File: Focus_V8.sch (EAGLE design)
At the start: 103 parts, among them X1 USB+SHIELD

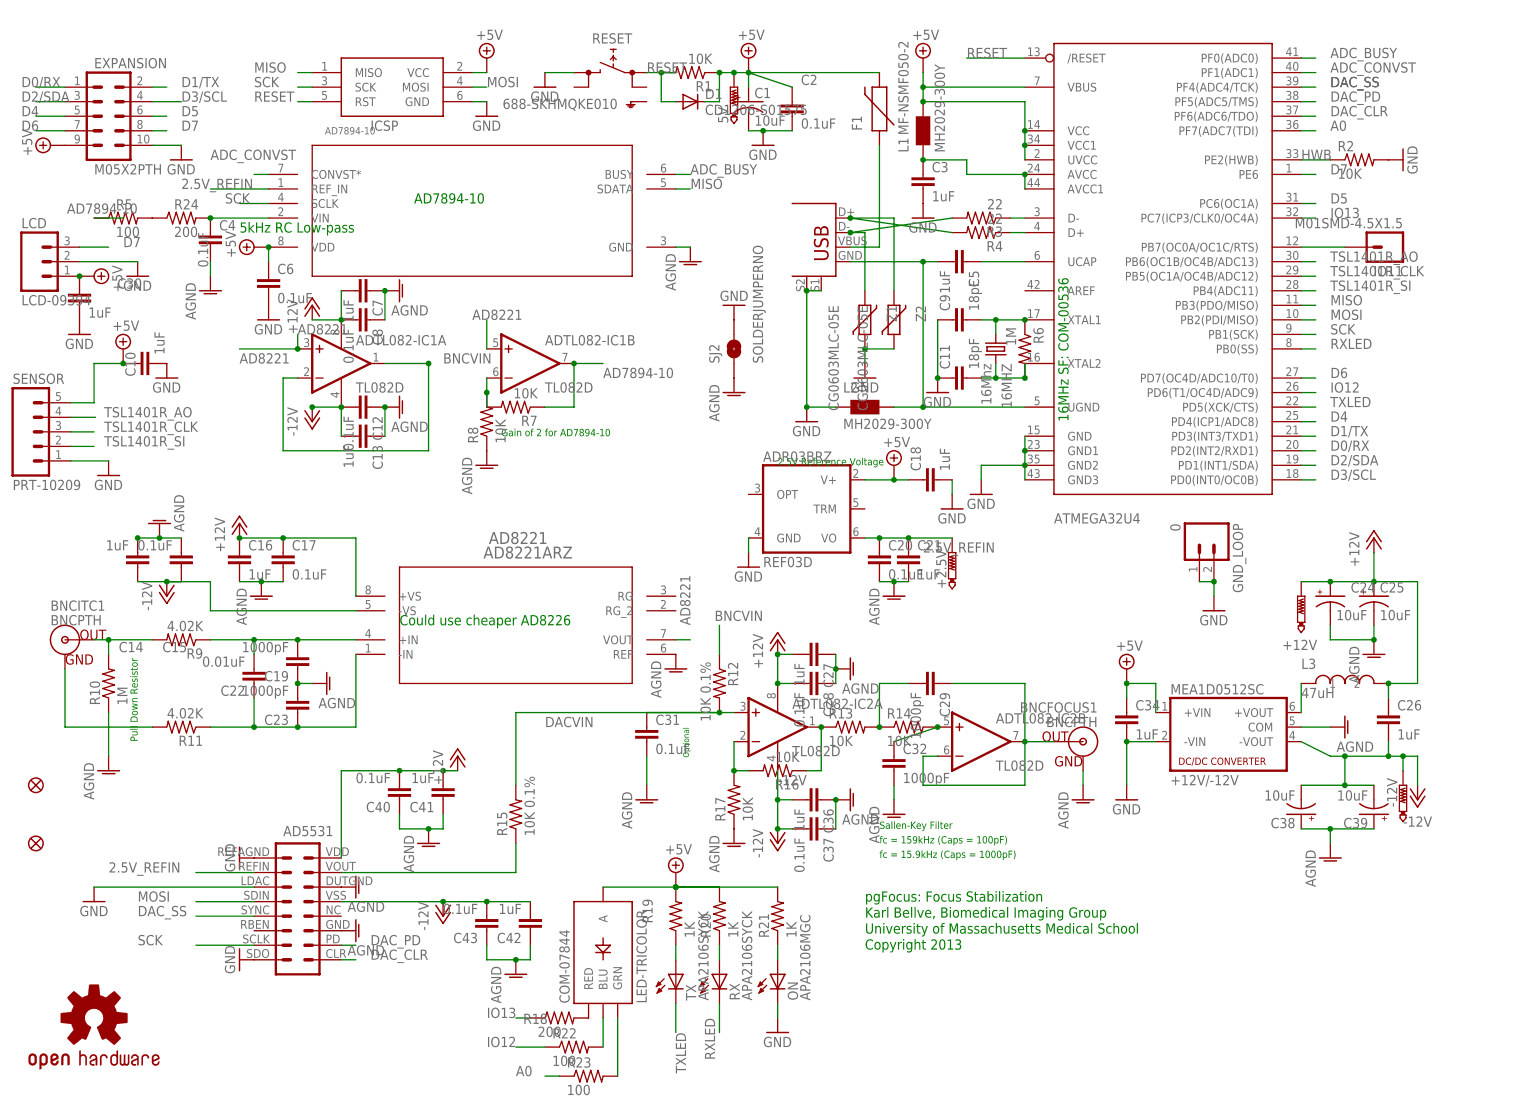
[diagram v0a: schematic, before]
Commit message: Changed connector for Expansion, cleaned up text
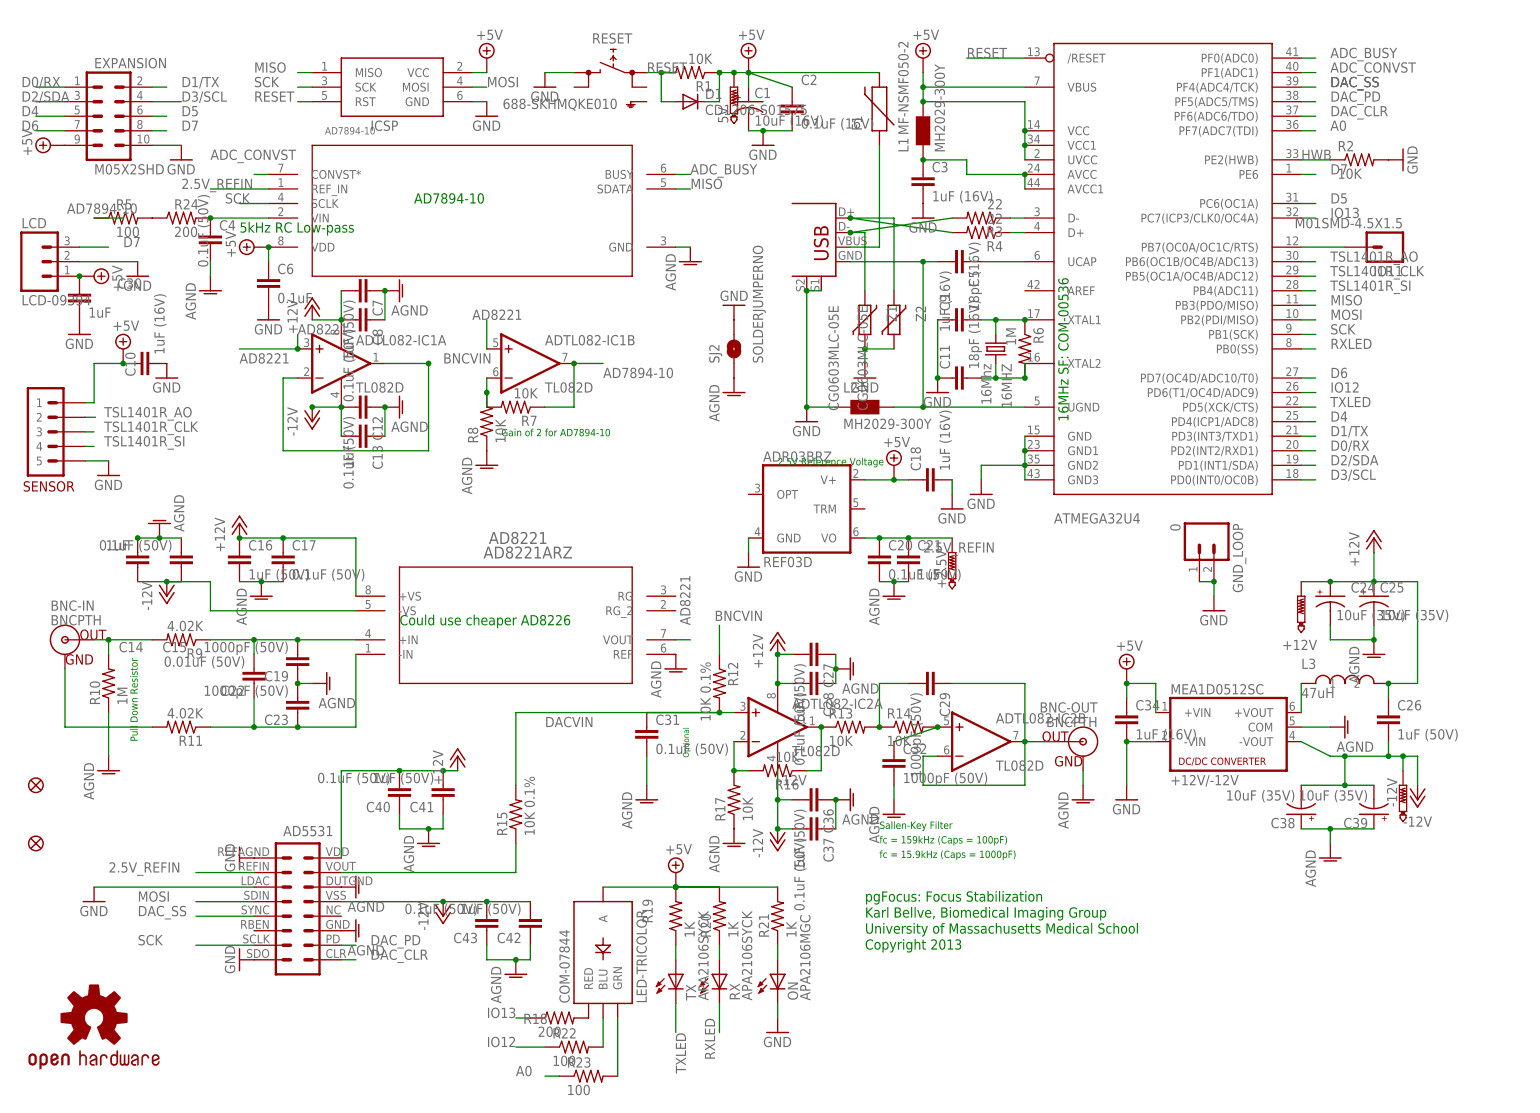
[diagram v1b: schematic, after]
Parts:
- C1: value 10uF -> 10uF (16V)
- C10, C18, C3, C34, C5: value 1uF -> 1uF (16V)
- C11, C9: value 18pF -> 18pF (16V)
- C12, C15, C17, C20, C28, C31, C37, C4, C40, C43, C8: value 0.1uF -> 0.1uF (50V)
- C16, C26, C27, C36, C41, C42, C7: value 1uF -> 1uF (50V)
- C19, C23, C29, C32: value 1000pF -> 1000pF (50V)
- C2: value 0.1uF -> 0.1uF (16V)
- C22: value 0.01uF -> 0.01uF (50V)
- C24, C25, C38, C39: value 10uF -> 10uF (35V)
- EXPANSION: value M05X2PTH -> M05X2SHD; device SparkFun:M05X2PTH -> SparkFun-Connectors:M05X2SHD
- SENSOR: value PRT-10209 -> M05; device SparkFun-Connectors:M05SMD2 -> BIG:M05
- renumbered BNCFOCUS1 to BNC-OUT, BNCITC1 to BNC-IN
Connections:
- net +5V: now also SENSOR.1; no longer SENSOR.5
- net GND: now also SENSOR.5; no longer SENSOR.1
- net TSL1401R_AO: now also SENSOR.2; no longer SENSOR.4
- net TSL1401R_SI: now also SENSOR.4; no longer SENSOR.2
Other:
- moved on the sheet: SENSOR

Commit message: Switchedd top two holes 1/8" Vias for mounting for chasis grounding
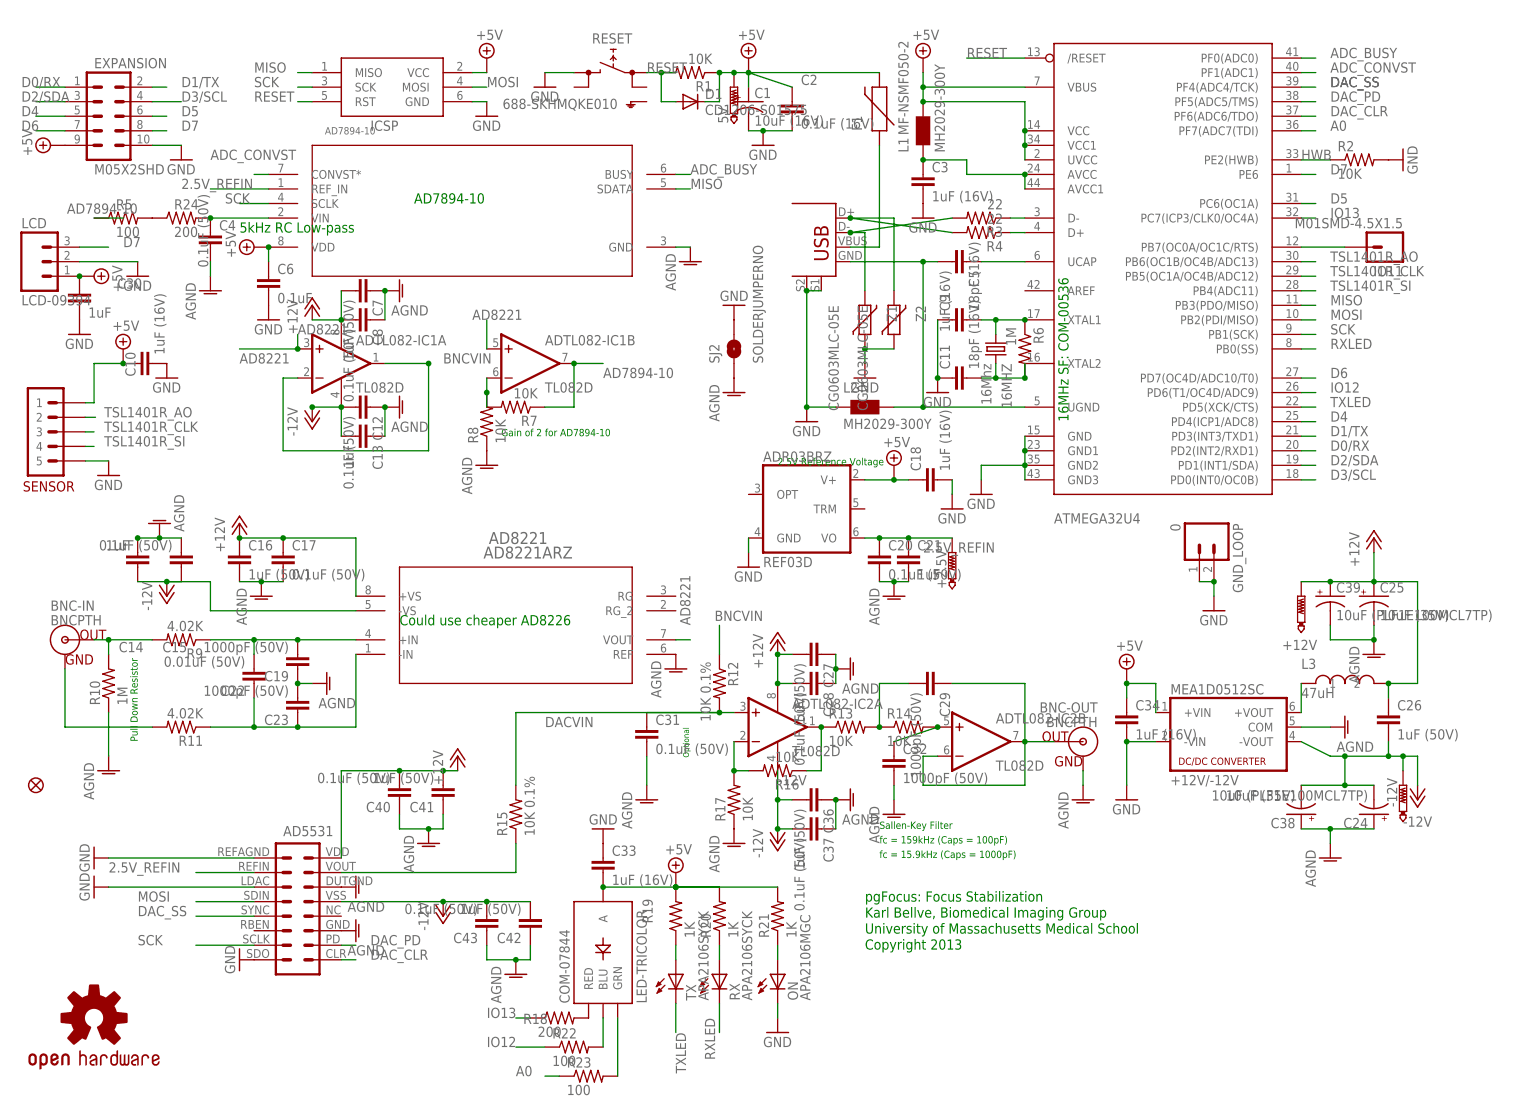
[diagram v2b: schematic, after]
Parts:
- removed JP2: FIDUCIAL1.5X3, SparkFun:FIDUCIAL1.5X3
- added C33: 1uF (16V), SparkFun:CAP0603-CAP
- C24, C39: value 10uF (35V) -> 10uF (PLF1E100MCL7TP); device SparkFun:CAP_POL1206-KIT -> SparkFun-Passives:CAP_POLPTH1
- renumbered X1 to USB
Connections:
- net +12V: now also C39.+; no longer C24.+
- net +5V: now also C33.2
- net -12V: now also C24.-; no longer C39.-
- net AGND: now also C24.+, C39.-; no longer C24.-, C39.+
- net GND: now also C33.1
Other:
- moved on the sheet: C24, C39
